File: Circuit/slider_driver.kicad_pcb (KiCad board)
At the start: 2 copper layers, 99.4 x 38.5 mm, 34 parts, among them IC1 ATTINY84A-SS, P1 5_PIN_SOCKET, P2 NEOPIXEL, P3 5_PIN_SOCKET, P4 I2C, P5 ISCP, P6 +12V, P7 GND, P8 +5V, P9 GND, SW1 RESET, U1 L9110, U2 RSA0N11M9A0J, U3 BREAK_CONNECTION, U4 74HC595-16-PIN, U5 74HC595-16-PIN

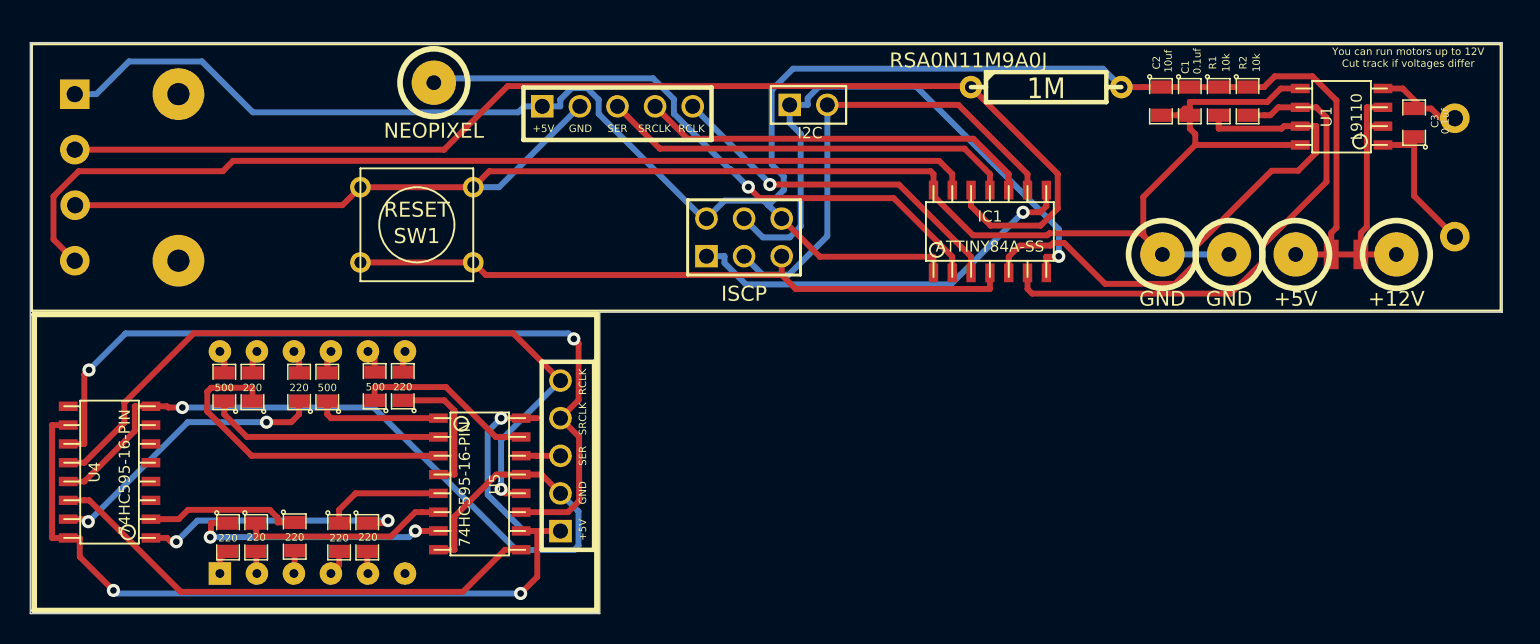
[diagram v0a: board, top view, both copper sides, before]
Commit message: fixed pin for iscp port
Total screw up there.
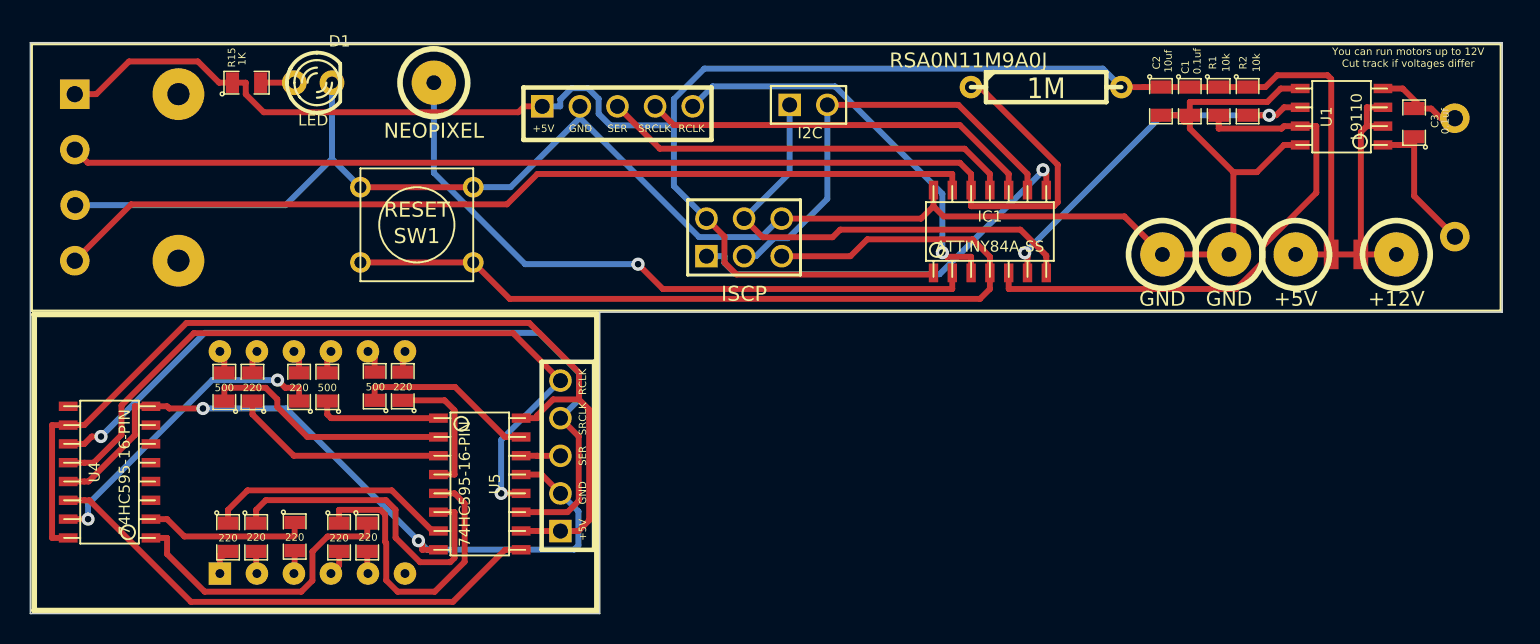
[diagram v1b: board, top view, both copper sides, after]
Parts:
- added D1: LED, LED-3MM, F.Cu at (31.1, 14.7)
- added R15: 1K, SM0805, F.Cu at (26.6, 14.7)
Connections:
- P5 pad 6: +12V -> GND
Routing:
- net N-0000047: track 45.6 -> 61.0 mm
- net N-0000024: track 8.07 -> 21.1 mm
- net N-0000052: track 35.4 -> 25.6 mm, vias 0 -> 2
- net N-0000054: track 39.9 -> 32.0 mm, vias 1 -> 0
- net N-0000029: track 13.9 -> 21.7 mm
- net N-0000025: track 22.2 -> 14.6 mm
- net N-0000018: track 57.9 -> 50.8 mm, vias 1 -> 2
- net N-0000050: track 68.1 -> 62.8 mm
- net N-0000019: track 63.9 -> 68.2 mm, vias 3 -> 0
- net N-0000016: track 56.5 -> 52.6 mm, vias 2 -> 1
- net N-0000048: track 41.8 -> 45.4 mm
- net N-0000020: track 24.1 -> 27.5 mm
- net +12V: track 147.1 -> 149.9 mm
- net N-0000053: track 32.6 -> 30.1 mm
- net N-0000035: track 0.00 -> 2.28 mm
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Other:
- board text added: "Controller for RSA0N11M9A0J motorised slider Designed by John Spencer, 2014 https://github.com/mage0r/RSA0N11M9A0J_motorised_slider Version 1.3"
- board text removed: "Controller for RSA0N11M9A0J motorised slider Designed by John Spencer, 2014 https://github.com/mage0r/RSA0N11M9A0J_motorised_slider Version 1.2"

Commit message: experimental motorslider
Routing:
- net +12V: track 149.9 -> 152.4 mm
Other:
- board text added: "1"
- board text added: "GND"
- board text added: "SDA"
- board text added: "SDC"
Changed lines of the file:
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@@
     (links 87)
     (no_connects 0)
-    (area 11.949999 11.949999 111.450001 50.600001)
+    (area 11.770999 11.22655 111.629001 50.794501)
     (thickness 1.6)
-    (drawings 9)
+    (drawings 13)
     (tracks 364)
     (zones 0)
@@
     (at 105.45 17.4 90)
     (attr smd)
-    (fp_text reference C3 (at 0.1 1.4 90) (layer F.SilkS)
-      (effects (font (size 0.50038 0.50038) (thickness 0.10922)))
-    )
-    (fp_text value 0.1uf (at 0.1 2.1 90) (layer F.SilkS)
+    (fp_text reference C3 (at -0.9 1.45 180) (layer F.SilkS)
+      (effects (font (size 0.50038 0.50038) (thickness 0.10922)))
+    )
+    (fp_text value 0.1uf (at -1.6 1.95 180) (layer F.SilkS)
       (effects (font (size 0.50038 0.50038) (thickness 0.10922)))
     )
@@
     )
   )
+  (gr_text SDC (at 65.8 14.6) (layer F.SilkS)
+    (effects (font (size 0.4 0.4) (thickness 0.1)))
+  )
+  (gr_text SDA (at 63.2 14.6) (layer F.SilkS)
+    (effects (font (size 0.4 0.4) (thickness 0.1)))
+  )
+  (gr_text GND (at 65.3 23.1) (layer F.SilkS)
+    (effects (font (size 0.7 0.7) (thickness 0.175)))
+  )
+  (gr_text 1 (at 55.7 26.5) (layer F.SilkS)
+    (effects (font (size 0.8 0.8) (thickness 0.2)))
+  )
   (gr_line (start 111.4 30.2) (end 50.45 30.2) (angle 90) (layer Edge.Cuts) (width 0.1))
   (gr_line (start 12 50.55) (end 12 12) (angle 90) (layer Edge.Cuts) (width 0.1))
@@
     (effects (font (size 1 1) (thickness 0.25)) (justify mirror))
   )
-  (segment (start 101.85 26.3) (end 101.85 18.0397) (width 0.4) (layer F.Cu) (net 1) (status 400000))
+  (segment (start 101.85 26.3) (end 101.85 18.0397) (width 0.4) (layer F.Cu) (net 1))
   (segment (start 101.85 18.0397) (end 102.2547 17.635) (width 0.4) (layer F.Cu) (net 1))
-  (segment (start 101.85 26.3) (end 104.25 26.3) (width 0.4) (layer F.Cu) (net 1) (status C00000))
-  (segment (start 94.2 14.9975) (end 95.4025 14.9975) (width 0.4) (layer F.Cu) (net 1) (status 400000))
-  (segment (start 99.85 14.45) (end 99.85 26.3) (width 0.4) (layer F.Cu) (net 1) (status 800000))
+  (segment (start 101.85 26.3) (end 104.25 26.3) (width 0.4) (layer F.Cu) (net 1))
+  (segment (start 94.2 14.9975) (end 95.4025 14.9975) (width 0.4) (layer F.Cu) (net 1))
+  (segment (start 99.85 14.45) (end 99.85 26.3) (width 0.4) (layer F.Cu) (net 1))
   (segment (start 99.6 14.2) (end 99.85 14.45) (width 0.4) (layer F.Cu) (net 1))
   (segment (start 96.2 14.2) (end 99.6 14.2) (width 0.4) (layer F.Cu) (net 1))
   (segment (start 95.4025 14.9975) (end 96.2 14.2) (width 0.4) (layer F.Cu) (net 1))
-  (segment (start 99.85 26.3) (end 101.85 26.3) (width 0.4) (layer F.Cu) (net 1) (status C00000))
+  (segment (start 99.85 26.3) (end 101.85 26.3) (width 0.4) (layer F.Cu) (net 1))
   (segment (start 99.85 26.3) (end 97.45 26.3) (width 0.4) (layer F.Cu) (net 1))
   (segment (start 92.25 14.9975) (end 90.3 14.9975) (width 0.4) (layer F.Cu) (net 1))
@@
   (segment (start 85.68 15) (end 87.1947 15) (width 0.4) (layer F.Cu) (net 1))
   (segment (start 88.35 14.9975) (end 87.1972 14.9975) (width 0.4) (layer F.Cu) (net 1))
-  (segment (start 23.3161 13.2674) (end 24.7487 14.7) (width 0.4) (layer F.Cu) (net 1))
-  (segment (start 18.6619 13.2674) (end 23.3161 13.2674) (width 0.4) (layer F.Cu) (net 1))
-  (segment (start 16.4543 15.475) (end 18.6619 13.2674) (width 0.4) (layer F.Cu) (net 1))
+  (segment (start 24.7161 17.9674) (end 24.7487 14.7) (width 0.4) (layer F.Cu) (net 1))
+  (segment (start 20.0619 17.9674) (end 24.7161 17.9674) (width 0.4) (layer F.Cu) (net 1))
+  (segment (start 16.4543 15.475) (end 20.0619 17.9674) (width 0.4) (layer F.Cu) (net 1))
   (segment (start 15 15.475) (end 16.4543 15.475) (width 0.4) (layer F.Cu) (net 1))
   (segment (start 25.6475 14.7) (end 24.7487 14.7) (width 0.4) (layer F.Cu) (net 1))

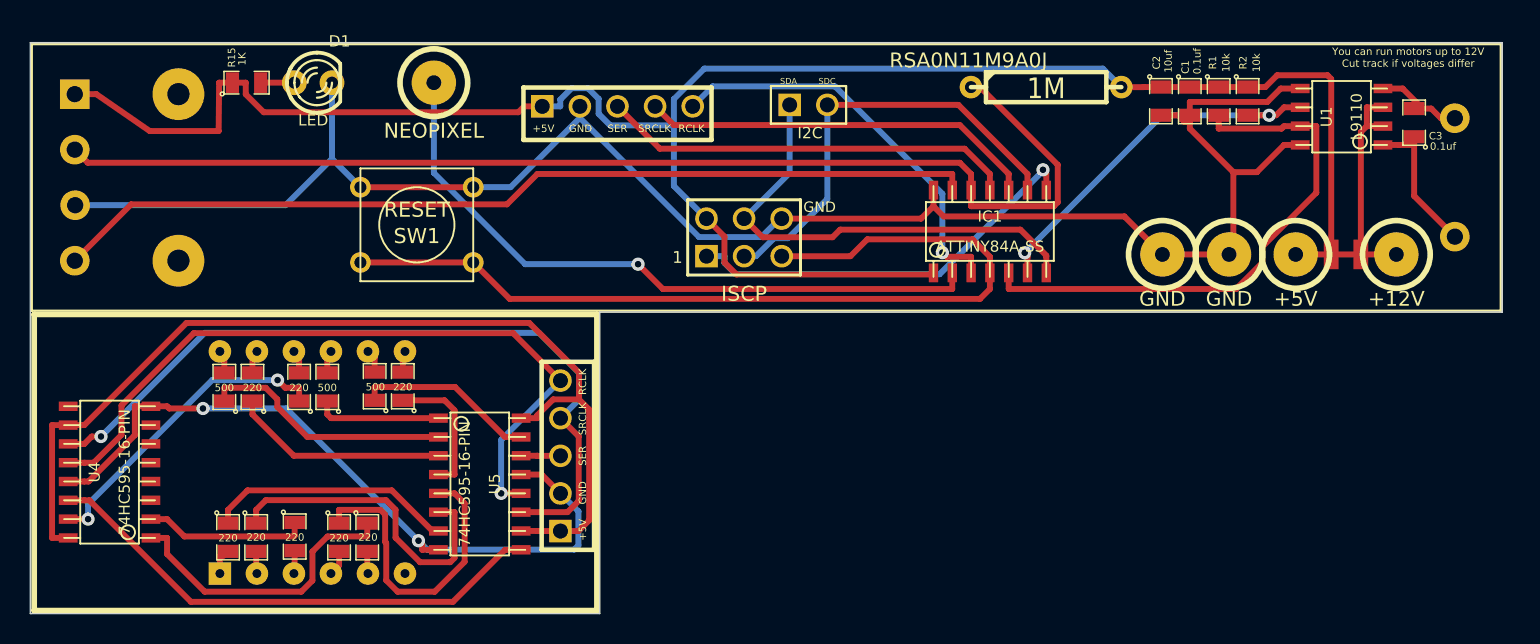
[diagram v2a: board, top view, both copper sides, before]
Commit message: Extra pins Re Bug #3
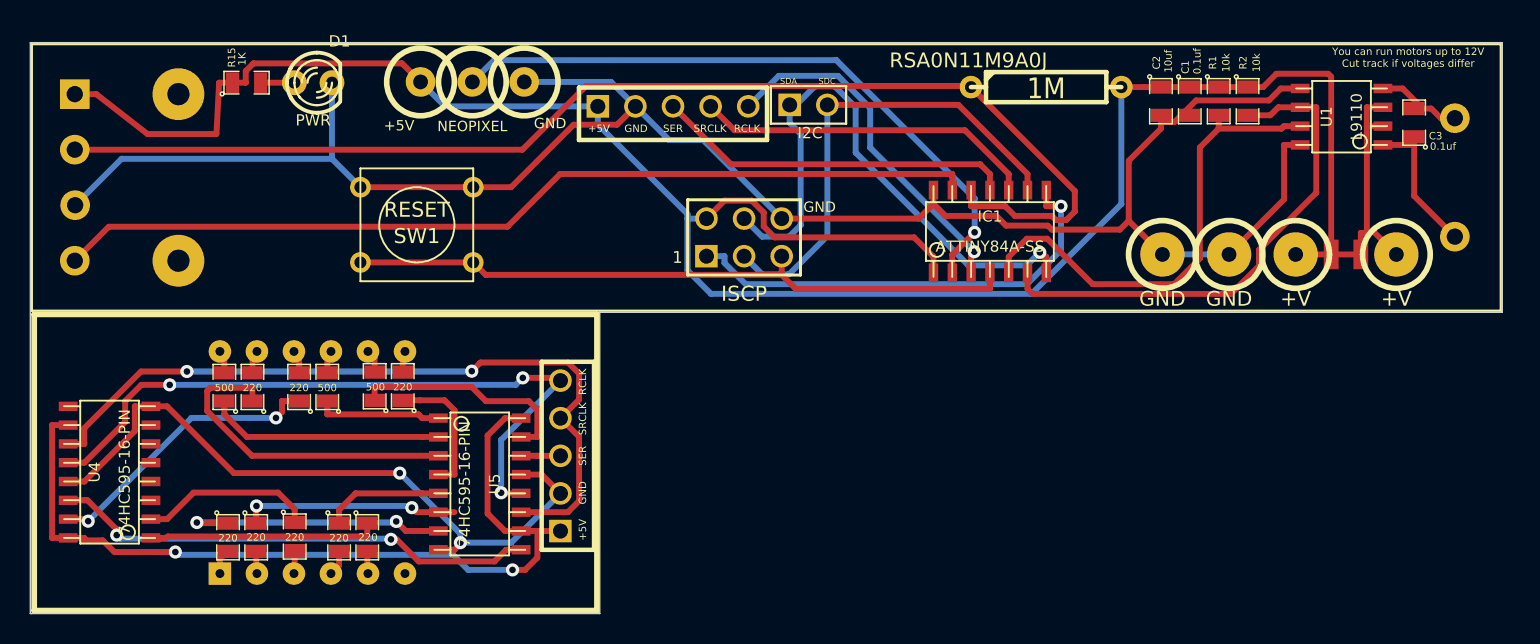
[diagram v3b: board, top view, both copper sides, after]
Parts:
- added P10: +5V, 1pin_slider, F.Cu at (38.4, 14.7)
- added P11: GND, 1pin_slider, F.Cu at (45.4, 14.7)
- D1: value LED -> PWR
- P6: value +12V -> +V
- P8: value +5V -> +V
- moved P1 3.75 mm to (55.4, 16.3)
- moved P2 2.60 mm to (41.9, 14.7)
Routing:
- net N-0000053: track 61.0 -> 45.6 mm
- net N-0000023: track 21.1 -> 8.07 mm
- net N-0000015: track 68.2 -> 58.2 mm, vias 0 -> 2
- net +12V: track 152.4 -> 162.1 mm
- net GND: track 121.4 -> 131.0 mm
- net N-0000052: track 25.6 -> 34.8 mm, vias 2 -> 0
- net N-0000024: track 14.6 -> 22.3 mm
- net N-0000054: track 32.0 -> 39.5 mm, vias 0 -> 1
- net N-0000028: track 21.7 -> 14.7 mm, vias 0 -> 2
- net N-0000051: track 37.2 -> 32.3 mm
- net N-0000021: track 20.3 -> 15.5 mm
- net N-0000014: track 50.8 -> 46.8 mm
- net N-0000047: track 28.1 -> 24.4 mm
- net N-0000017: track 26.9 -> 23.1 mm
- net N-0000016: track 27.5 -> 24.1 mm
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
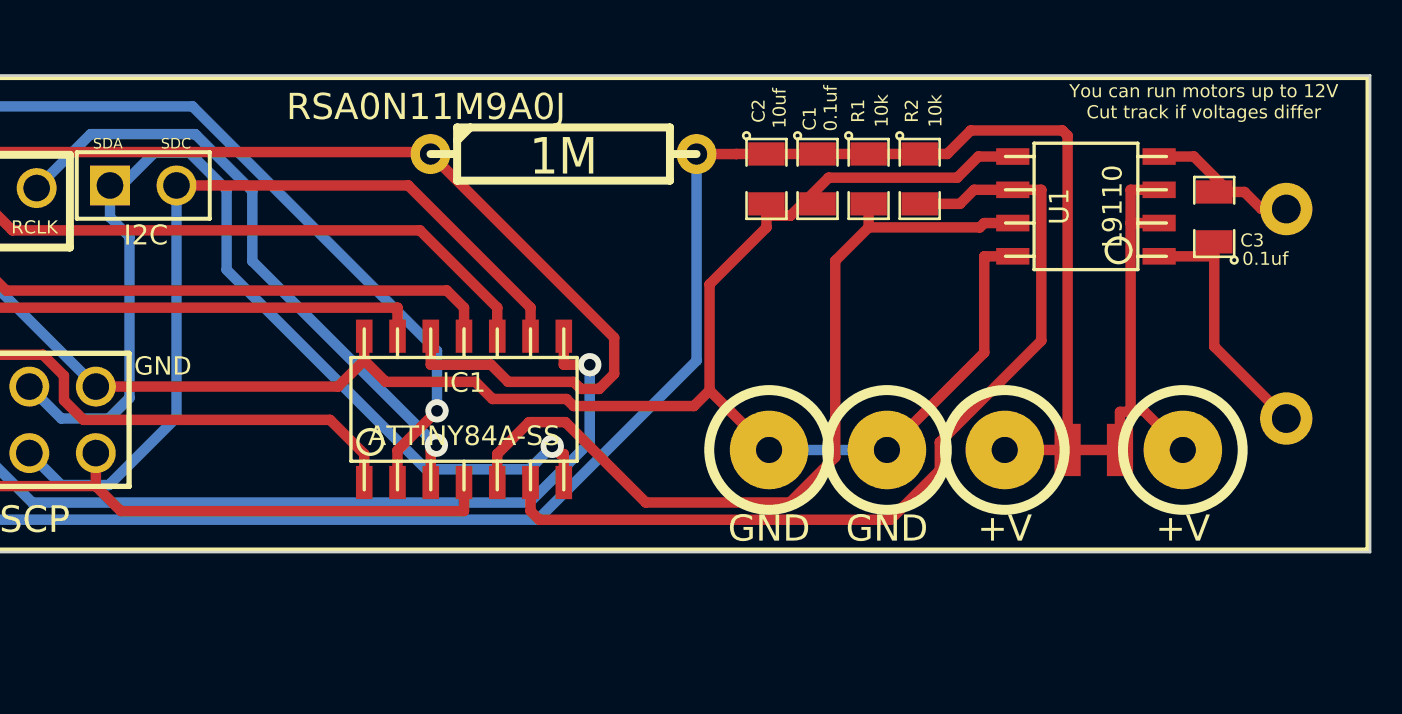
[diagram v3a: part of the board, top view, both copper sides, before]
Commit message: i2c support added into arduino
No idea what I changed in the pcb :)
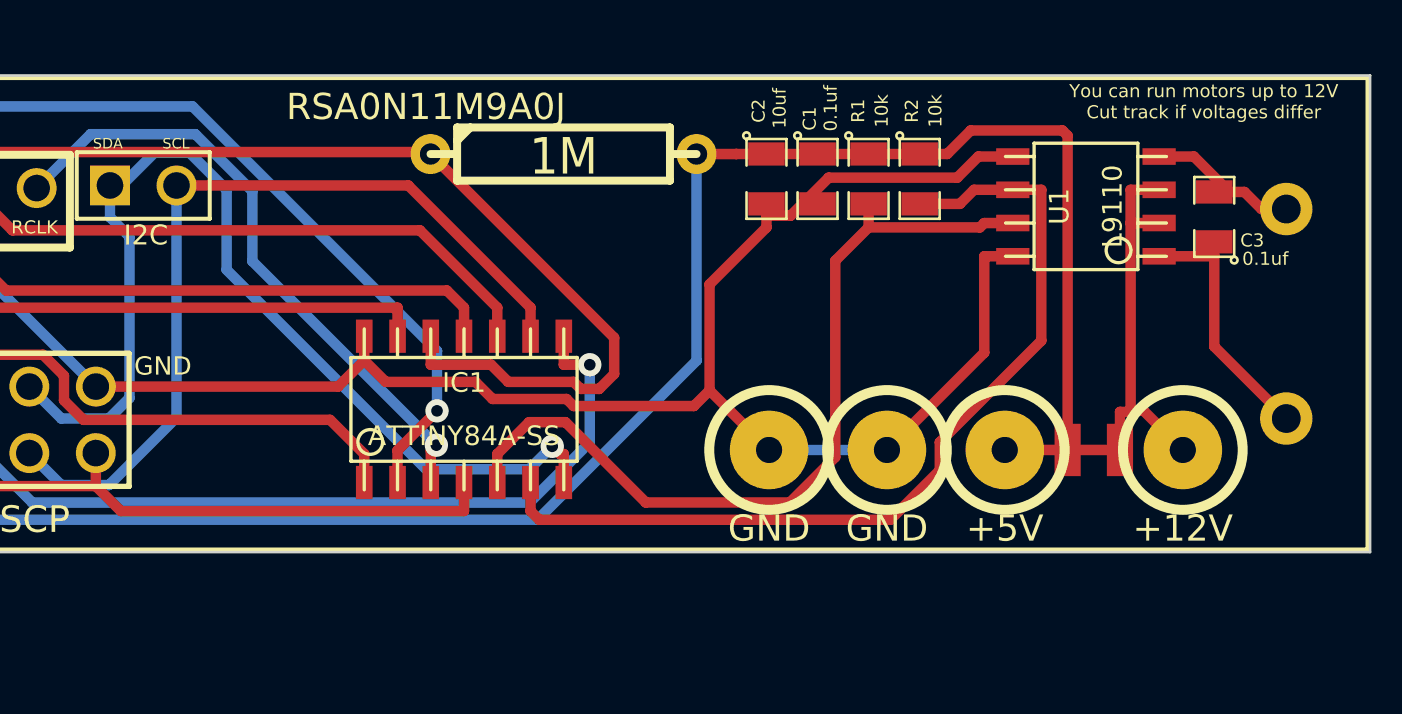
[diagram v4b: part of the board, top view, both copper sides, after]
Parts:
- P6: value +V -> +12V
- P8: value +V -> +5V
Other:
- board text added: "SCL"
- board text removed: "SDC"
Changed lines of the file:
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@@
     (links 89)
     (no_connects 0)
-    (area 11.949999 11.949999 111.450001 50.600001)
+    (area 11.770999 10.661 111.629001 50.794501)
     (thickness 1.6)
     (drawings 13)
@@
       (effects (font (size 1.016 1.016) (thickness 0.254)))
     )
-    (fp_text value +V (at 0 3) (layer F.SilkS)
+    (fp_text value +12V (at 0 3) (layer F.SilkS)
       (effects (font (size 1 1) (thickness 0.15)))
     )
@@
       (effects (font (size 1.016 1.016) (thickness 0.254)))
     )
-    (fp_text value +V (at 0 3) (layer F.SilkS)
+    (fp_text value +5V (at 0 3) (layer F.SilkS)
       (effects (font (size 1 1) (thickness 0.15)))
     )
@@
     )
   )
-  (gr_text SDC (at 65.8 14.6) (layer F.SilkS)
+  (gr_text SCL (at 65.8 14.6) (layer F.SilkS)
     (effects (font (size 0.4 0.4) (thickness 0.1)))
   )
